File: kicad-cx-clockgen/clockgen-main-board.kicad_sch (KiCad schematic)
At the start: 15 parts, among them J1 Headswitch_SMA, J2 Conn_Coaxial, J3 Conn_01x03_Pin, J4 Conn_01x03_Pin, U1 Pico

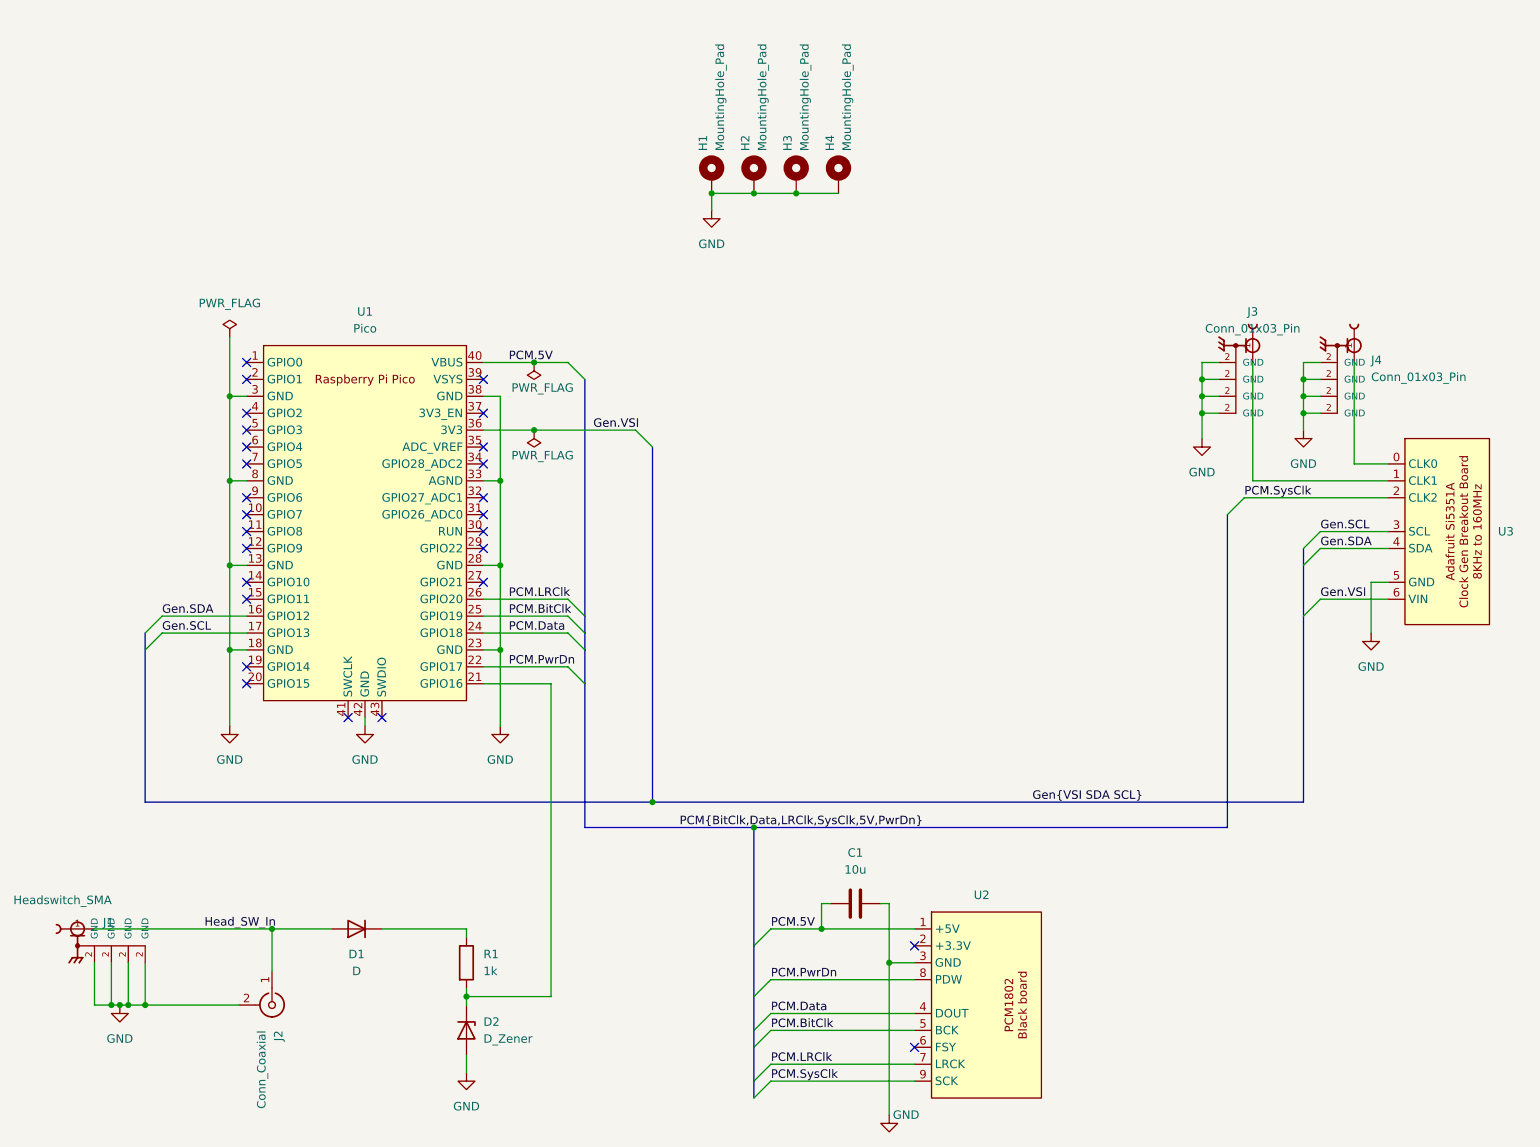
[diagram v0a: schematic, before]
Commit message: refactor: Split combined main board + jig project into discrete ones
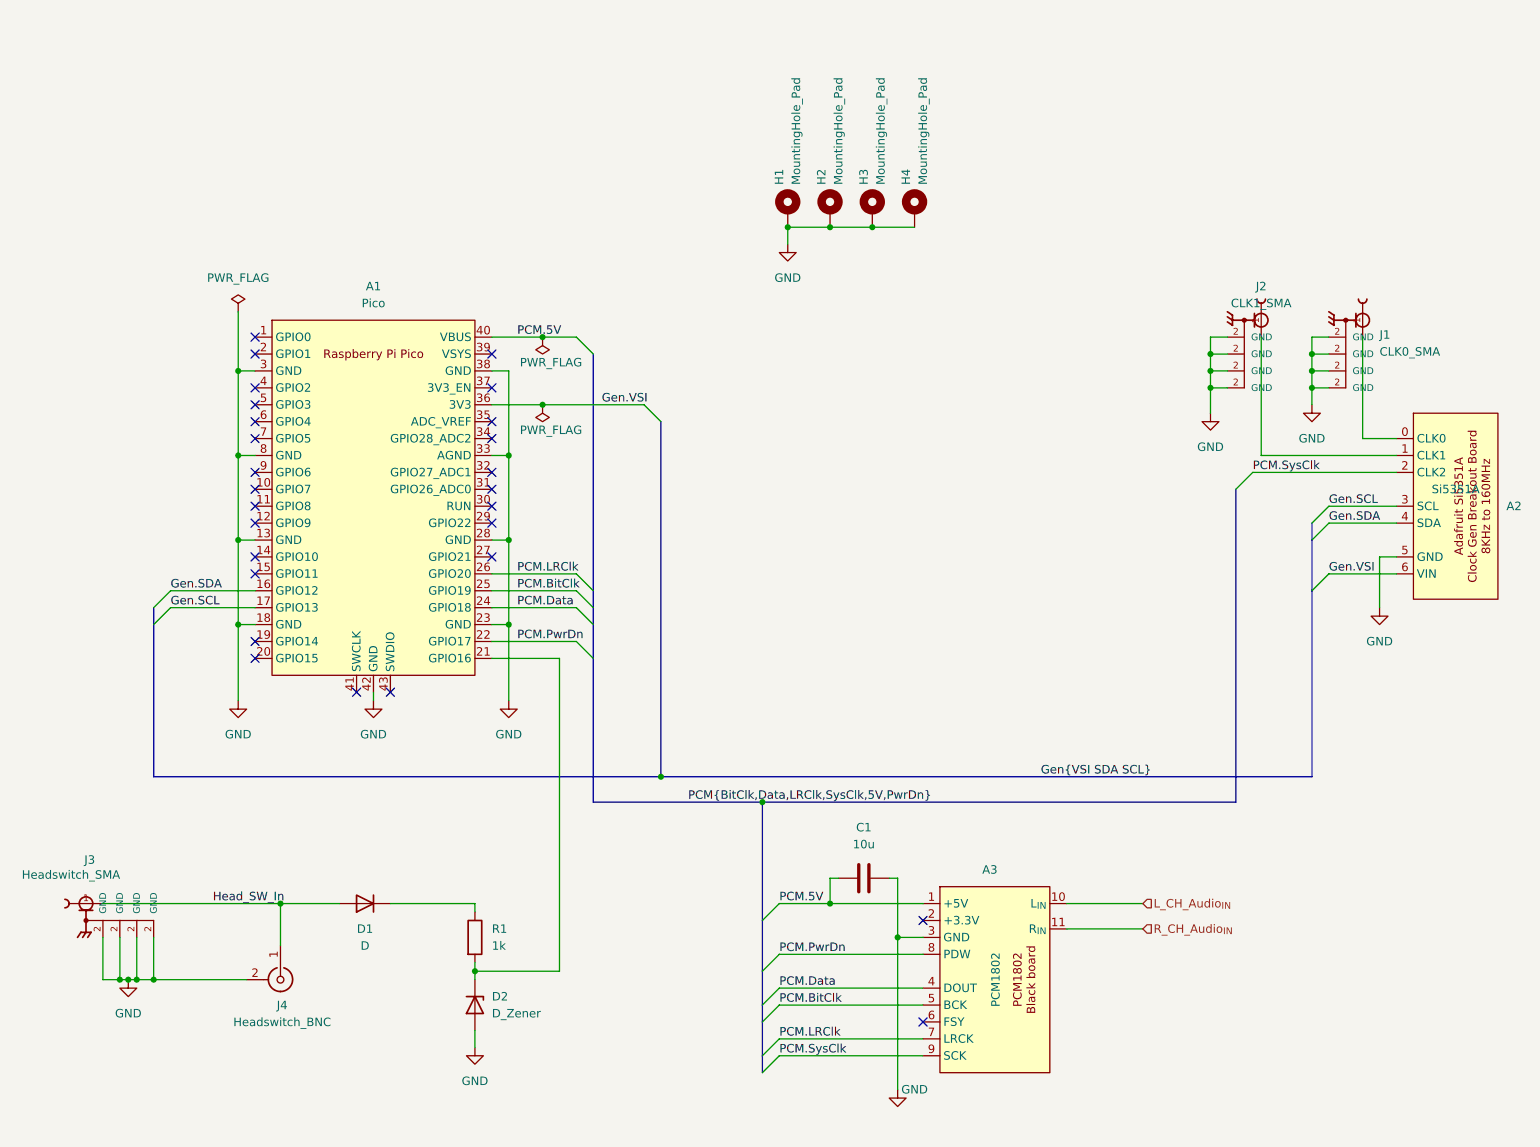
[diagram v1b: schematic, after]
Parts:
- removed J2: Conn_Coaxial, GDH Connectors:Molex_0731000154_BNC_RA_THT, symbol Connector:Conn_Coaxial
- removed J4: Conn_01x03_Pin, GDH Connectors:GRADCONN_RFPC-SMA28-F, symbol GDH Connectors:RFPC-SMA28-F
- removed U1: Pico, GDH Modules:Pi_Pico_SMD_TH, symbol GDH Modules:Raspberry Pi Pico
- removed U2: (no value), GDH Modules:black-pcm1802-board, symbol GDH Modules:black-pcm1802-board
- removed U3: (no value), GDH Modules:Adafruit_Si5351A_Breakout_Board, symbol GDH Modules:Adafruit_Si5351A
- added A1: Pico, GDH Modules:Pi_Pico_SMD_TH, symbol GDH Modules:Raspberry Pi Pico
- added A2: Si5351A, GDH Modules:Adafruit_Si5351A_Breakout_Board, symbol GDH Modules:Adafruit_Si5351A
- added A3: PCM1802, GDH Modules:black-pcm1802-board, symbol GDH Modules:black-pcm1802-board
- added J2: CLK1_SMA, GDH Connectors:GRADCONN_RFPC-SMA28-F, symbol GDH Connectors:RFPC-SMA28-F
- added J4: Headswitch_BNC, GDH Connectors:Molex_0731000154_BNC_RA_THT, symbol Connector:Conn_Coaxial
- J1: value Headswitch_SMA -> CLK0_SMA
- J3: value Conn_01x03_Pin -> Headswitch_SMA
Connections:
- net GND: now also A1.13 (GND), A1.18 (GND), A1.23 (GND), A1.28 (GND), A1.3 (GND), A1.33 (AGND), A1.38 (GND), A1.42 (GND), A1.8 (GND), A2.5 (GND), A3.3 (GND), J2.2 (GND), J4.2 (Ext)
- net Gen.SCL: now also A1.17 (GPIO13), A2.3 (SCL)
- net Gen.SDA: now also A1.16 (GPIO12), A2.4 (SDA)
- net Gen.VSI: now also A1.36 (3V3), A2.6 (VIN)
- net Head_SW_In: now also J3.1, J4.1 (In); no longer J1.1
- net PCM.5V: now also A1.40 (VBUS), A3.1 (+5V)
- net PCM.BitClk: now also A1.25 (GPIO19), A3.5 (BCK)
- net PCM.Data: now also A1.24 (GPIO18), A3.4 (DOUT)
- net PCM.LRClk: now also A1.26 (GPIO20), A3.7 (LRCK)
- net PCM.PwrDn: now also A1.22 (GPIO17), A3.8 (PDW)
- net PCM.SysClk: now also A2.2 (CLK2), A3.9 (SCK)
- net at D2.1 (K), R1.2: now also A1.21 (GPIO16)
- new net: A2.1 (CLK1), J2.1
- new net: A2.0 (CLK0), J1.1
- new net L_CH_Audio_{IN}: A3.10 (L_{IN})
- new net R_CH_Audio_{IN}: A3.11 (R_{IN})
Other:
- title: Main Board -> ${proj-title}
